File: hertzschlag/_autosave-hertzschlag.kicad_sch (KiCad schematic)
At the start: 27 parts, among them IC1 TB67H450FNG,EL, IC2 TB67H450FNG,EL, J1 TB_1X2, J2 MotorA, J3 MotorB, J4 Conn_01x30_Pin, J5 Conn_01x04_Female, J6 Conn_01x03_Male, J7 Conn_01x03_Male, SW1 SW_Push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

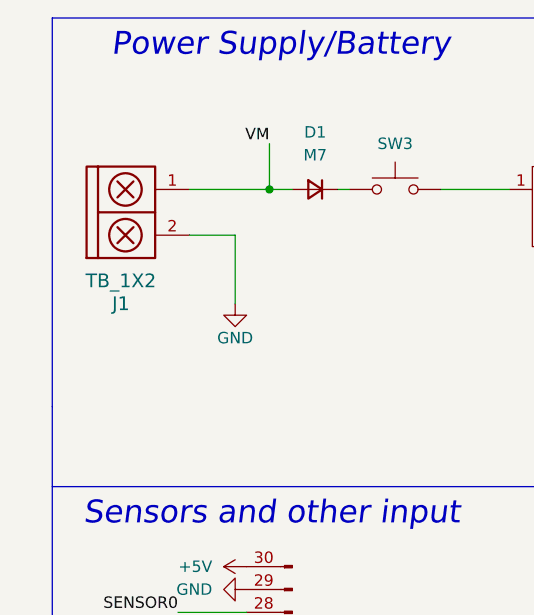
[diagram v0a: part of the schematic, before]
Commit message: Updated PCB design
Changes to XT30 Connector and routing.
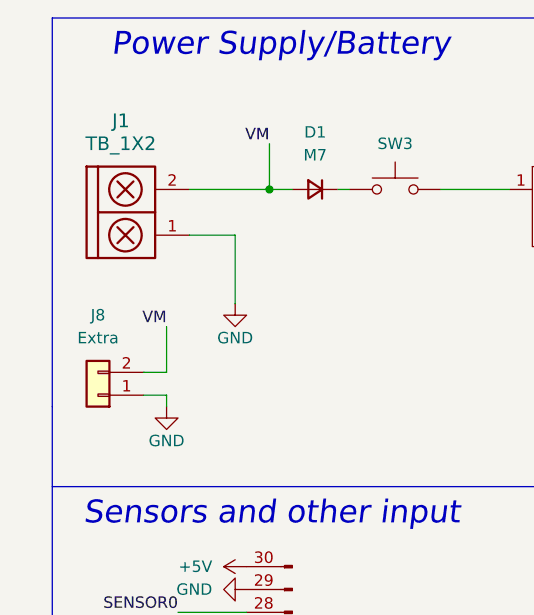
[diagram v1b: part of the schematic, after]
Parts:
- added J8: Extra, Connector_PinSocket_2.54mm:PinSocket_1x02_P2.54mm_Vertical, symbol Connector_Generic:Conn_01x02
- J1: footprint Connector_PinHeader_2.54mm:PinHeader_1x02_P2.54mm_Horizontal -> Connector_AMASS:AMASS_XT30U-F_1x02_P5.0mm_Vertical
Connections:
- net GND: now also J1.1, J8.1 (Pin_1); no longer J1.2
- net VM: now also J1.2, J8.2 (Pin_2); no longer J1.1
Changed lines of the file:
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@@
 	(wire
 		(pts
+			(xy 25.4 54.61) (xy 25.4 55.88)
+		)
+		(stroke
+			(width 0)
+			(type default)
+		)
+	)
+	(wire
+		(pts
 			(xy 78.74 31.75) (xy 93.98 31.75)
 		)
@@
 	(wire
 		(pts
+			(xy 25.4 46.99) (xy 25.4 52.07)
+		)
+		(stroke
+			(width 0)
+			(type default)
+		)
+	)
+	(wire
+		(pts
 			(xy 157.48 41.91) (xy 157.48 43.18)
 		)
@@
 	(wire
 		(pts
+			(xy 22.86 54.61) (xy 25.4 54.61)
+		)
+		(stroke
+			(width 0)
+			(type default)
+		)
+	)
+	(wire
+		(pts
 			(xy 157.48 55.88) (xy 157.48 52.07)
 		)
@@
 	(wire
 		(pts
+			(xy 22.86 52.07) (xy 25.4 52.07)
+		)
+		(stroke
+			(width 0)
+			(type default)
+		)
+	)
+	(wire
+		(pts
 			(xy 133.35 41.91) (xy 133.35 36.83)
 		)
@@
 		)
 	)
+	(label "VM"
+		(at 25.4 46.99 180)
+		(effects
+			(font
+				(size 1.27 1.27)
+			)
+			(justify right bottom)
+		)
+	)
 	(label "SDA"
 		(at 260.35 73.66 0)
@@
 	)
 	(symbol
+		(lib_id "power:GND")
+		(at 25.4 55.88 0)
+		(unit 1)
+		(exclude_from_sim no)
+		(in_bom yes)
+		(on_board yes)
+		(dnp no)
+		(property "Reference" "#PWR018"
+			(at 25.4 62.23 0)
+			(effects
+				(font
+					(size 1.27 1.27)
+				)
+				(hide yes)
+			)
+		)
+		(property "Value" "GND"
+			(at 25.4 59.69 0)
+			(effects
+				(font
+					(size 1.27 1.27)
+				)
+			)
+		)
+		(property "Footprint" ""
+			(at 25.4 55.88 0)
+			(effects
+				(font
+					(size 1.27 1.27)
+				)
+				(hide yes)
+			)
+		)
+		(property "Datasheet" ""
+			(at 25.4 55.88 0)
+			(effects
+				(font
+					(size 1.27 1.27)
+				)
+				(hide yes)
+			)
+		)
+		(property "Description" "Power symbol creates a global label with name \"GND\" , ground"
+			(at 25.4 55.88 0)
+			(effects
+				(font
+					(size 1.27 1.27)
+				)
+				(hide yes)
+			)
+		)
+		(pin "1"
+		)
+		(instances
+			(project "hertzschlag"
+				(path "/f154c6d1-45a5-4a23-92c8-ac7beedeed65"
+					(reference "#PWR018")
+					(unit 1)
+				)
+			)
+		)
+	)
+	(symbol
 		(lib_id "power:+5V")
 		(at 34.29 104.14 90)
@@
 		(lib_id "EESTN5:TB_1X2")
 		(at 19.05 34.29 0)
-		(mirror x)
 		(unit 1)
 		(exclude_from_sim no)
@@
 		(dnp no)
 		(property "Reference" "J1"
-			(at 20.32 44.45 0)
+			(at 20.32 24.13 0)
 			(effects
 				(font
@@
 		)
 		(property "Value" "TB_1X2"
-			(at 20.32 41.91 0)
+			(at 20.32 26.67 0)
 			(effects
 				(font
@@
 			)
 		)
-		(property "Footprint" "Connector_PinHeader_2.54mm:PinHeader_1x02_P2.54mm_Horizontal"
-			(at 20.32 47.244 0)
+		(property "Footprint" "Connector_AMASS:AMASS_XT30U-F_1x02_P5.0mm_Vertical"
+			(at 20.32 21.336 0)
 			(effects
 				(font
@@
 		)
 		(property "Datasheet" ""
-			(at 17.78 35.56 0)
+			(at 17.78 33.02 0)
 			(effects
 				(font
@@
 					(unit 1)
 				)
+			)
+		)
+	)
+	(symbol
+		(lib_id "Connector_Generic:Conn_01x02")
+		(at 17.78 54.61 180)
+		(unit 1)
+		(exclude_from_sim no)
+		(in_bom yes)
+		(on_board yes)
+		(dnp no)
+		(fields_autoplaced yes)
+		(property "Reference" "J8"
+			(at 17.78 45.72 0)
+			(effects
+				(font
+					(size 1.27 1.27)
+				)
+			)
+		)
+		(property "Value" "Extra"
+			(at 17.78 48.26 0)
+			(effects
+				(font
+					(size 1.27 1.27)
+				)
+			)
+		)
+		(property "Footprint" "Connector_PinSocket_2.54mm:PinSocket_1x02_P2.54mm_Vertical"
+			(at 17.78 54.61 0)
+			(effects
+				(font
+					(size 1.27 1.27)
+				)
+				(hide yes)
+			)
+		)
+		(property "Datasheet" "~"
+			(at 17.78 54.61 0)
+			(effects
+				(font
+					(size 1.27 1.27)
+				)
+				(hide yes)
+			)
+		)
+		(property "Description" "Generic connector, single row, 01x02, script generated (kicad-library-utils/schlib/autogen/connector/)"
+			(at 17.78 54.61 0)
+			(effects
+				(font
+					(size 1.27 1.27)
+				)
+				(hide yes)
+			)
+		)
+		(pin "1"
+		)
+		(pin "2"
+		)
+		(instances
+			(project ""
+				(path "/f154c6d1-45a5-4a23-92c8-ac7beedeed65"
+					(reference "J8")
+					(unit 1)
+				)
